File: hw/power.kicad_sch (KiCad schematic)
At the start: 72 parts, among them J1 Ext_Power, J11 PEN_SEL, J2 USB_C_Receptacle_USB2.0, J3 Jtag_Master, J9 Expansion, Q1 Si3477, Q2 Si3477, U1 TLV62569DDC, U16 74LVC1G32, U2 TLV62569DDC, U3 TLV62569DDC, U4 FT240XS

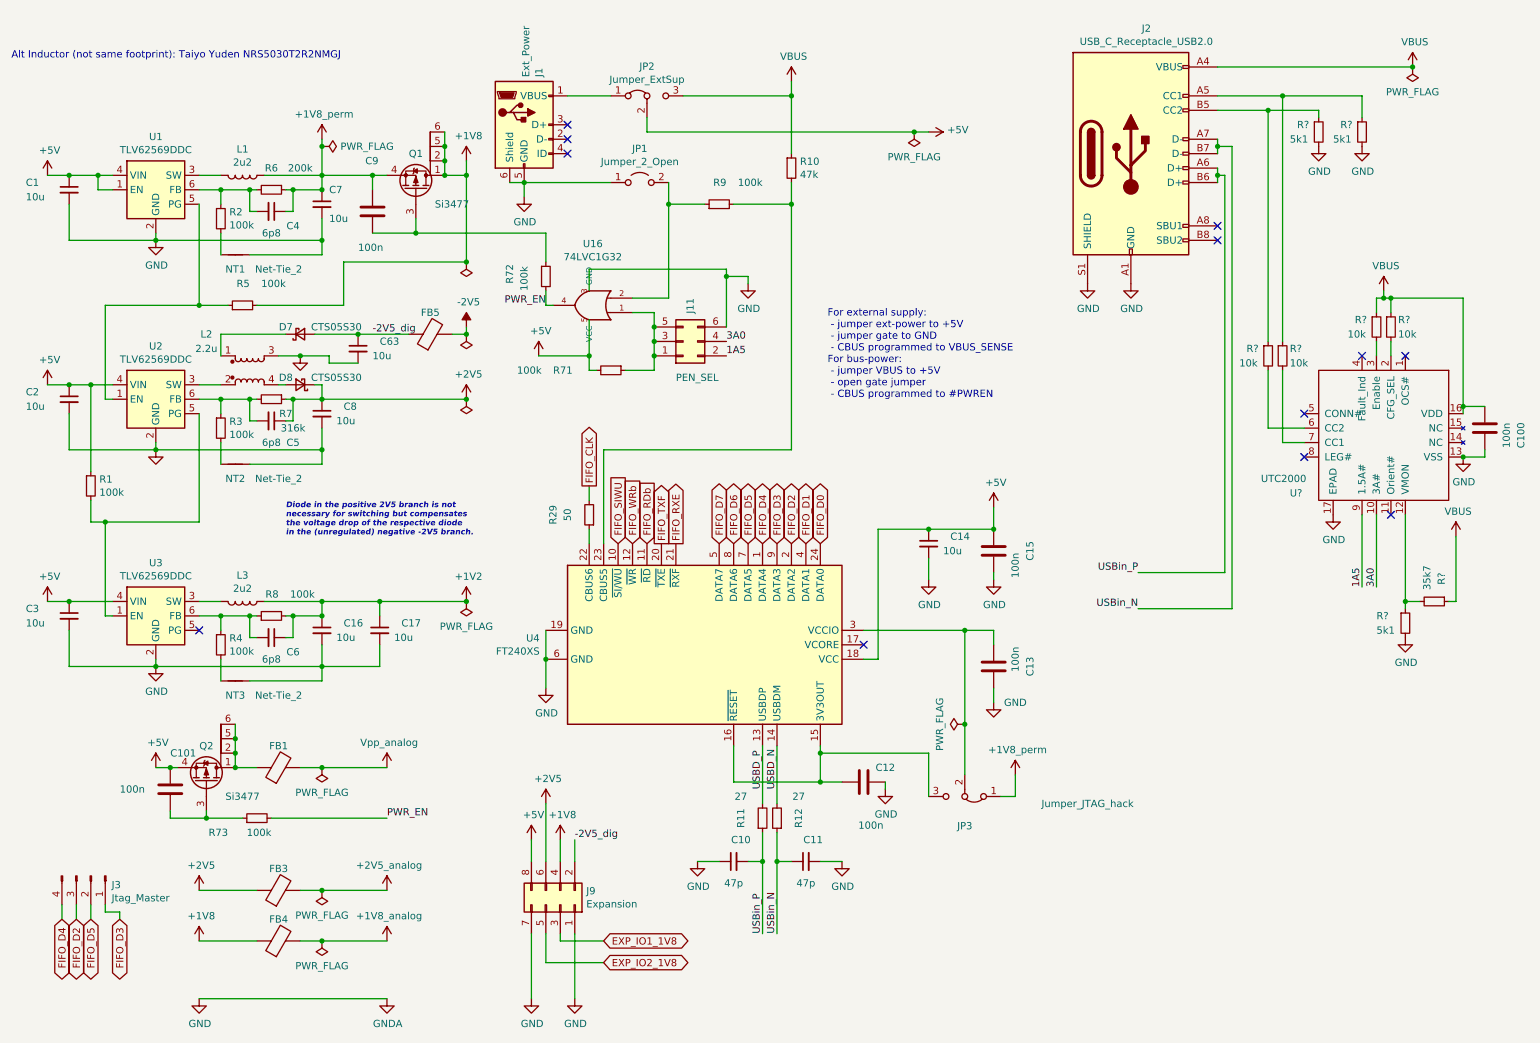
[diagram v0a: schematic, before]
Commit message: basic schematic, started layout (placing first components)
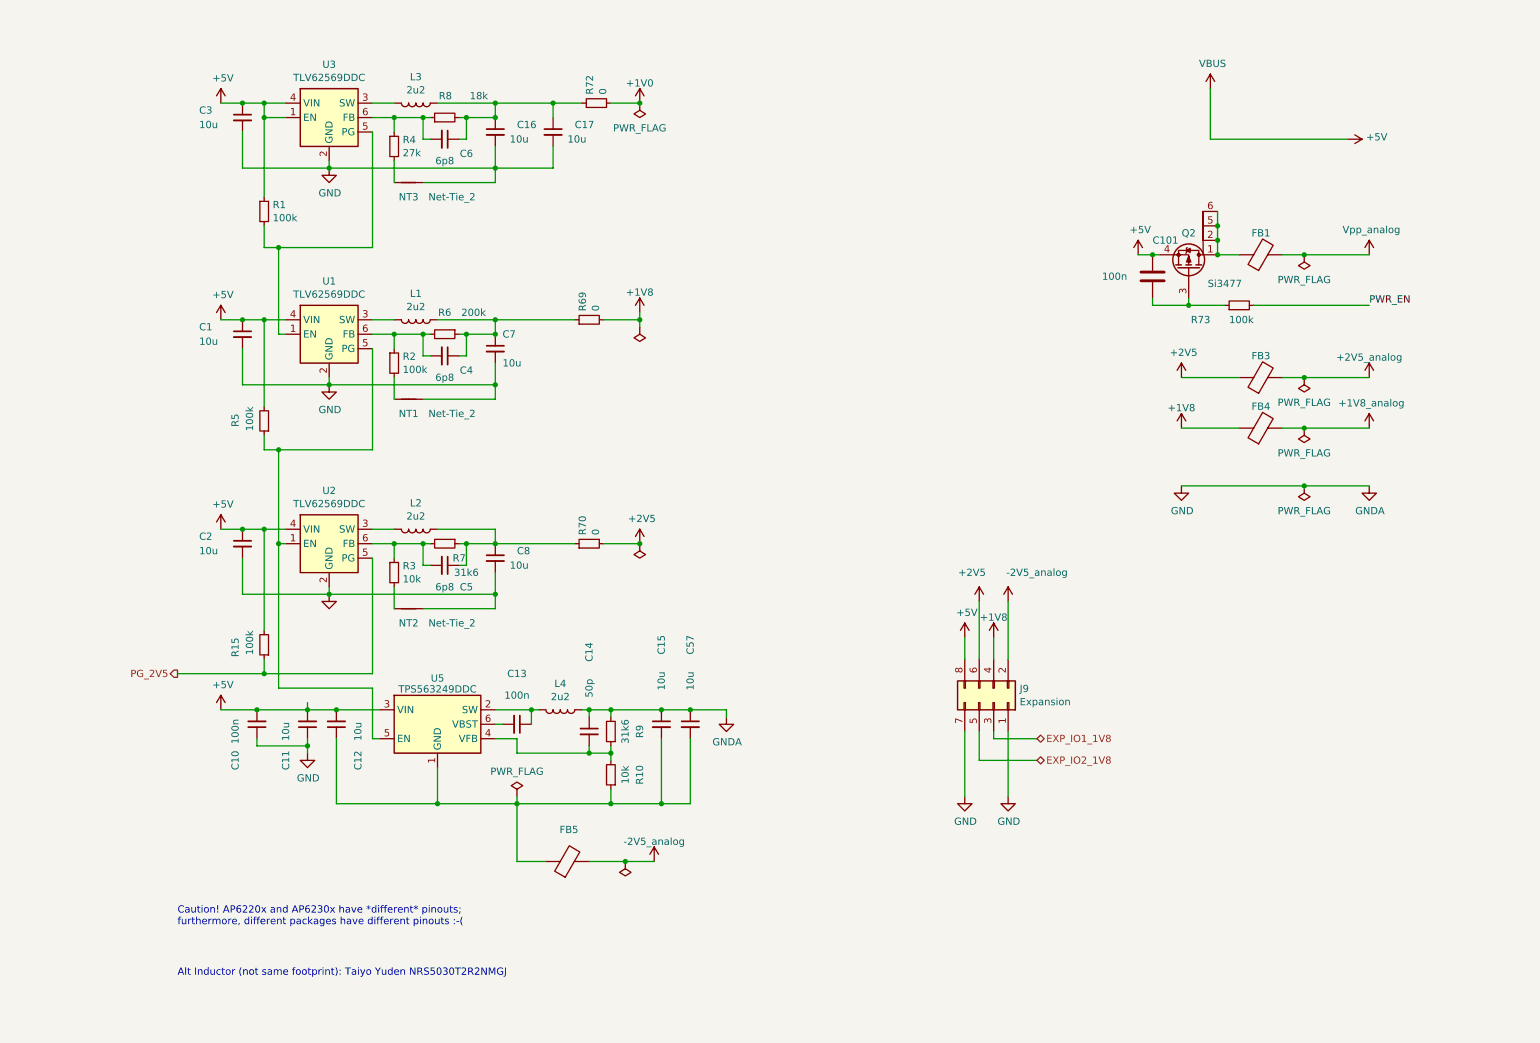
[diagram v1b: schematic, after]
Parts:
- removed C100, C12, C13, C15, C9: 100n, Capacitor_SMD:C_0603_1608Metric, symbol fmc:100nF_603
- removed C63: 10u, Capacitor_SMD:C_1206_3216Metric, symbol Device:C_Small
- removed D7: CTS05S30, proj_footprints:sod323, symbol Device:D_Schottky_Small
- removed D8: CTS05S30, proj_footprints:sod323-special, symbol Device:D_Schottky_Small
- removed J1: Ext_Power, Connector_USB:USB_Micro-B_Molex-105017-0001, symbol Connector:USB_B_Micro
- removed J11: PEN_SEL, Connector_PinHeader_2.54mm:PinHeader_2x03_P2.54mm_Vertical, symbol Connector_Generic:Conn_02x03_Odd_Even
- removed J2: USB_C_Receptacle_USB2.0, proj_footprints:USB_C_Receptacle_GCT_USB4085_smaller_holes, symbol Connector:USB_C_Receptacle_USB2.0
- removed J3: Jtag_Master, Connector_PinHeader_2.54mm:PinHeader_1x04_P2.54mm_Vertical, symbol usbadc-rescue:Conn_01x04_Male-Connector
- removed JP1: Jumper_2_Open, Connector_PinHeader_2.54mm:PinHeader_1x02_P2.54mm_Vertical, symbol Jumper:Jumper_2_Open
- removed JP2: Jumper_ExtSup, Connector_PinHeader_2.54mm:PinHeader_1x03_P2.54mm_Vertical, symbol usbadc-rescue:Jumper_3_Bridged12-Jumper
- removed JP3: Jumper_JTAG_hack, Connector_PinHeader_2.54mm:PinHeader_1x03_P2.54mm_Vertical, symbol usbadc-rescue:Jumper_3_Bridged12-Jumper
- removed L2: 2.2u, proj_footprints:L_Taiyo-Yuden_NR-50xx+bourns0703, symbol Device:L_Coupled_1324
- removed Q1: Si3477, Package_TO_SOT_SMD:TSOT-23-6, symbol fmc:Q_PMOS_DDGSDD
- removed R11, R12: 27, Resistor_SMD:R_0603_1608Metric, symbol Device:R_Small
- removed R29: 50, Resistor_SMD:R_0402_1005Metric, symbol Device:R_Small
- removed R71: 100k, Resistor_SMD:R_0603_1608Metric, symbol Device:R_Small
- removed R? (x4): 10k, Resistor_SMD:R_0603_1608Metric, symbol Device:R_Small
- removed R? (x3): 5k1, Resistor_SMD:R_0603_1608Metric, symbol Device:R_Small
- removed R?: 35k7, Resistor_SMD:R_0603_1608Metric, symbol Device:R_Small
- removed U16: 74LVC1G32, Package_TO_SOT_SMD:SOT-353_SC-70-5, symbol fmc:74LVC1G32
- removed U4: FT240XS, Package_SO:SSOP-24_3.9x8.7mm_P0.635mm, symbol fmc:FT240XS
- removed U?: UTC2000, Package_DFN_QFN:QFN-16-1EP_3x3mm_P0.5mm_EP1.75x1.75mm_ThermalVias, symbol fmc:UTC2000
- added C12, C15, C57: 10u, Capacitor_SMD:C_1206_3216Metric, symbol Device:C_Small
- added C13: 100n, Capacitor_SMD:C_0603_1608Metric, symbol Device:C_Small
- added L2, L4: 2u2, Inductor_SMD:L_Taiyo-Yuden_NR-50xx, symbol Device:L
- added R15: 100k, Resistor_SMD:R_0603_1608Metric, symbol Device:R_Small
- added R69, R70: 0, Resistor_SMD:R_0603_1608Metric, symbol Device:R_Small
- added U5: TPS563249DDC, Package_TO_SOT_SMD:SOT-23-6, symbol Regulator_Switching:TPS563240DDC
- C10: value 47p -> 100n; Manufacturer Wurth -> (none); Part 885012006055 -> (none)
- C11: value 47p -> 10u; footprint Capacitor_SMD:C_0603_1608Metric -> Capacitor_SMD:C_1206_3216Metric; Manufacturer Wurth -> (none); Part 885012006055 -> (none)
- C14: value 10u -> 50p; footprint Capacitor_SMD:C_1206_3216Metric -> Capacitor_SMD:C_0603_1608Metric; Manufacturer TDK -> (none); Part CNC5L1X7R1C106K160AE -> (none)
- FB1, FB3, FB4, FB5: symbol usbadc-rescue:Ferrite_Bead-Device -> Device:FerriteBead
- NT1, NT2, NT3: symbol usbadc-rescue:Net-Tie_2-Device -> Device:NetTie_2
- R10: value 47k -> 10k; Manufacturer Yageo -> (none); Part RC0603FR-07100KL -> (none)
- R3: value 100k -> 10k
- R4: value 100k -> 27k
- R7: value 316k -> 31k6
- R72: value 100k -> 0
- R8: value 100k -> 18k
- R9: value 100k -> 31k6; Manufacturer Yageo -> (none); Part RC0603FR-07100KL -> (none)
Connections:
- net +1V2 is gone; now on an unnamed net: C16.1, C17.1, C6.1, L3.1, R8.2
- net USBin_N is gone; now on net GND: C11.1
- net USBin_P is gone; now on net +5V: C10.2
- net VBUS is gone; now on an unnamed net: R10.1
- net +1V8: now also R69.2; no longer R5.2
- net +2V5: now also R70.2; no longer C5.1, C8.1, R7.1
- net +5V: now also C11.2, R5.2, U3.1 (EN), C12.2, R15.2, U5.3 (VIN); no longer C14.1, U1.1 (EN)
- net GND: now also C14.1, R9.2, C15.1, C57.1, L4.1; no longer C11.2, C14.2
- net PWR_EN: no longer R72.2
- net at R5.1, U1.5 (PG), U2.1 (EN): now also U5.5 (EN)
- net at U2.3 (SW): now also L2.2
- net at U3.5 (PG): now also R1.2, U1.1 (EN)
- net at R9.1: now also C14.2, R10.2, U5.4 (VFB)
- net +1V8_perm: no longer names the net of C4.1, C7.1, L1.1, R6.1
- net +1V8_perm: now also R69.1
- net -2V5 renamed -2V5_analog
- net -2V5_analog: now also J9.2 (Pin_2)
- net -2V5_dig: no longer names the net of FB5.1
- net -2V5_dig: now also C12.1, C15.2, C57.2, U5.1 (GND); no longer J9.2 (Pin_2)
- new net: C5.1, C8.1, L2.1, R7.1, R70.1
- new net: C13.1, L4.2, U5.2 (SW)
- new net: C13.2, U5.6 (VBST)
- new net +1V0: R72.2
- new net PG_2V5: R15.1, U2.5 (PG)
- no-connect marks 12 -> 0
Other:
- note added: "Caution! AP6220x and AP6230x have *different* pinouts; furthermore, different packages have different pinouts :-("
- note removed: "Diode in the positive 2V5 branch is not necessary for switching but compensates the voltage drop of the respective diode in the (unregulated) negative -2V5 branch."
- note removed: "For external supply: - jumper ext-power to +5V - jumper gate to GND - CBUS programmed to VBUS_SENSE For bus-power: - jumper VBUS to +5V - open gate jumper - CBUS programmed to #PWREN"
- moved on the sheet: C1, C101, C16, C17, C2, C3, C4, C5, C6, C7, C8, FB1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

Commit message: WIP - a lot already laid out.
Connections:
- net +5V_switched: now reaches FB1.1, Q2.1 (D), Q2.2 (D), Q2.5 (D), Q2.6 (D)
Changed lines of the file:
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@@
   (junction (at 214.63 58.42) (diameter 0) (color 0 0 0 0)
   )
+  (junction (at 226.06 50.8) (diameter 0) (color 0 0 0 0)
+  )
   (junction (at 58.42 132.08) (diameter 0) (color 0 0 0 0)
   )
@@
     (stroke (width 0) (type default))
   )
+  (wire (pts (xy 226.06 50.8) (xy 252.73 50.8))
+    (stroke (width 0) (type default))
+  )
   (wire (pts (xy 114.3 138.43) (xy 115.57 138.43))
     (stroke (width 0) (type default))
@@
   )
   (wire (pts (xy 99.06 138.43) (xy 105.41 138.43))
+    (stroke (width 0) (type default))
+  )
+  (wire (pts (xy 252.73 50.8) (xy 252.73 48.895))
     (stroke (width 0) (type default))
   )
@@
         )
       )
+    )
+  )
+  (symbol (lib_id "fmc:+5V_switched") (at 252.73 48.895 0) (unit 1)
+    (in_bom yes) (on_board yes) (dnp no) (fields_autoplaced)
+    (property "Reference" "#PWR09" (at 252.73 52.705 0)
+      (effects (font (size 1.27 1.27)) hide)
+    )
+    (property "Value" "+5V_switched" (at 252.73 45.3931 0)
+      (effects (font (size 1.27 1.27)))
+    )
+    (property "Footprint" "" (at 252.73 48.895 0)
+      (effects (font (size 1.27 1.27)) hide)
+    )
+    (property "Datasheet" "" (at 252.73 48.895 0)
+      (effects (font (size 1.27 1.27)) hide)
+    )
+    (pin "1")
+    (instances
+      (project "usbadc"
+        (path "/7c8a1f8d-8834-4c9b-aaae-1f231e9b09a1/00000000-0000-0000-0000-00006086f2e3"
+          (reference "#PWR09") (unit 1)
+        )
+      )

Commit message: layout finished (draft)
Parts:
- removed C101: 100n, Capacitor_SMD:C_0603_1608Metric, symbol fmc:100nF_603
- removed C17: 10u, Capacitor_SMD:C_1206_3216Metric, symbol Device:C_Small
- removed NT1, NT2, NT3: Net-Tie_2, NetTie:NetTie-2_SMD_Pad0.5mm, symbol Device:NetTie_2
- removed Q2: Si3477, Package_TO_SOT_SMD:TSOT-23-6, symbol fmc:Q_PMOS_DDGSDD
- removed R70: 0, Resistor_SMD:R_0603_1608Metric, symbol Device:R_Small
- added C17: 100n, Capacitor_SMD:C_0603_1608Metric, symbol fmc:100nF_603
- added C28: 10u, Capacitor_SMD:C_1206_3216Metric, symbol Device:C_Small
- added Q8: DMC2053UVT, Package_TO_SOT_SMD:TSOT-23-6, symbol Transistor_FET:DMC2053UVT
- L1, L2, L3, L4: value 2u2 -> 1u5; footprint Inductor_SMD:L_Taiyo-Yuden_NR-50xx -> Inductor_SMD:L_1008_2520Metric; Manufacturer Bourns -> (none); Part SRN8040TA-2R2Y -> (none)
- U1, U2, U3: value TLV62569DDC -> RT8096B; Manufacturer Texas Instruments -> Richtek; Part TLV62569PDDC -> RT8096B
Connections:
- net +1V8: now also J9.6 (Pin_6); no longer J9.4 (Pin_4)
- net +1V8_analog: now also C17.2, C28.1
- net +2V5_analog: now also J9.4 (Pin_4)
- net +5V: now also R73.1, Q8.2 (S)
- net +5V_switched: now also Q8.4 (D)
- net GND: now also R2.2, R3.2, R4.2, C17.1, C28.2, Q8.5 (S)
- net at C5.1, C8.1, L2.1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: now also FB3.1
- removed net +2V5: FB3.1, J9.6 (Pin_6)
- net PG_2V5 renamed 5V_EN
- net 5V_EN: now also Q8.1 (G)
- net PWR_EN: no longer names the net of R73.2
- net PWR_EN: now also Q8.3 (G), Q8.6 (D)
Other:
- note removed: "Alt Inductor (not same footprint): Taiyo Yuden NRS5030T2R2NMGJ"
- moved on the sheet: FB3, R73

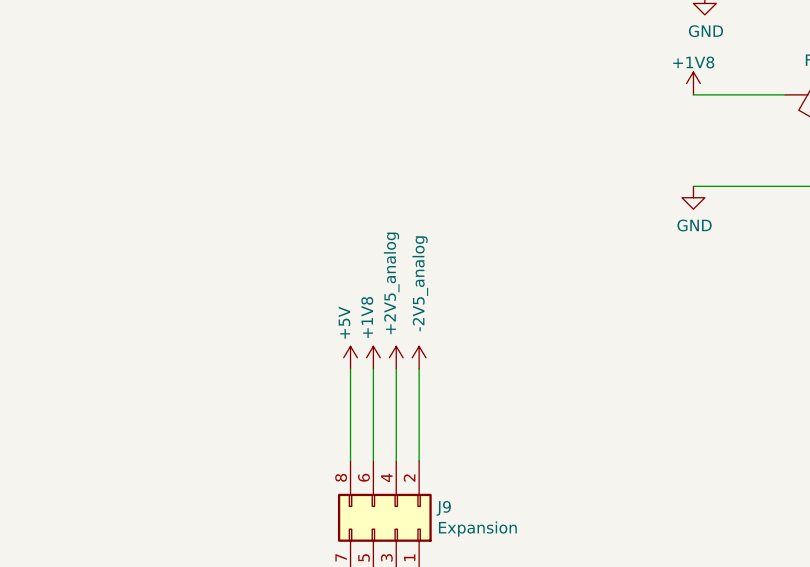
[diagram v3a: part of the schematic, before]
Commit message: finished routing; DRC passes (except for 1 hole violation at push-button)
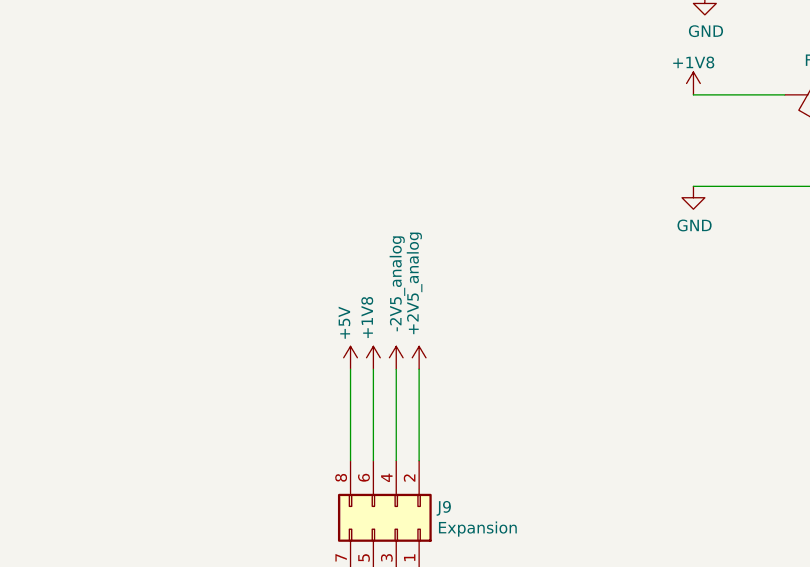
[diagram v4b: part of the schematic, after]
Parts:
- C1, C16, C2, C3, C7, C8: Manufacturer TDK -> (none); Part CNC5L1X7R1C106K160AE -> (none)
- C17: Manufacturer Murata -> (none); Part GCJ188R71E104KA12D -> (none)
- R1, R15, R2, R3, R4, R5, R69, R72, R73, R8: Manufacturer Yageo -> (none); Part RC0603FR-07100KL -> (none)
- R6: Manufacturer Panasonic -> (none); Part ERJ-3EKF2003V -> (none)
- R7: Manufacturer Yageo -> (none); Part RC0603FR-07316KL -> (none)
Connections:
- net +2V5_analog: now also J9.2 (Pin_2); no longer J9.4 (Pin_4)
- net -2V5_analog: now also J9.4 (Pin_4); no longer J9.2 (Pin_2)

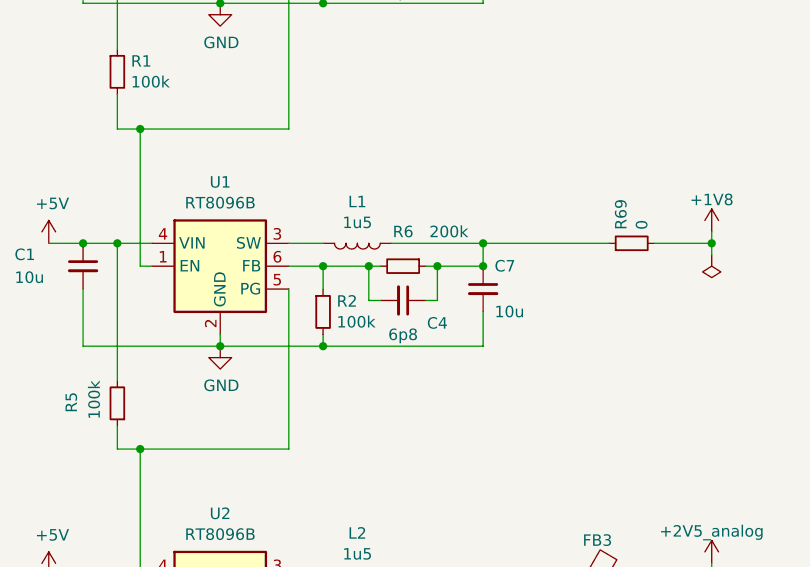
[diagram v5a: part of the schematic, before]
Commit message: standardized resistor/capacitor values
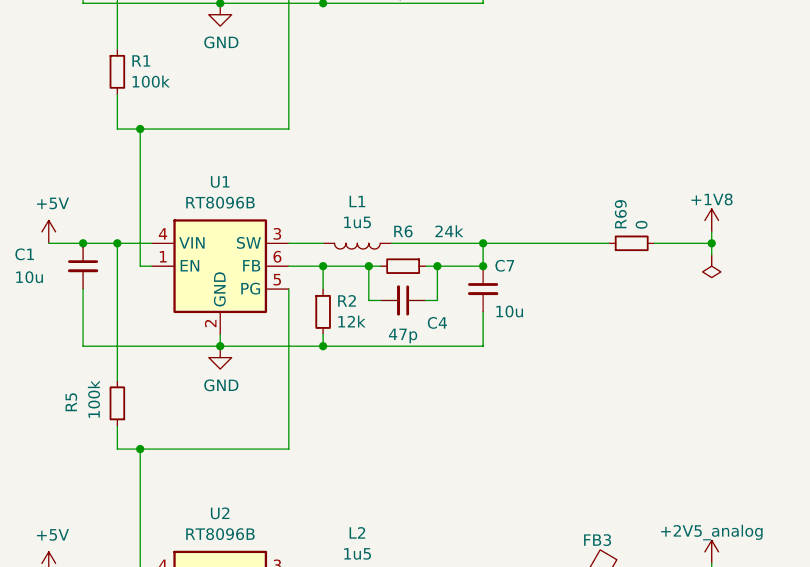
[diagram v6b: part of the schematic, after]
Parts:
- C4: value 6p8 -> 47p
- R2: value 100k -> 12k
- R6: value 200k -> 24k
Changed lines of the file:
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@@
       (effects (font (size 1.27 1.27)) (justify left))
     )
-    (property "Value" "100k" (at 82.7786 78.613 0)
+    (property "Value" "12k" (at 82.7786 78.613 0)
       (effects (font (size 1.27 1.27)) (justify left))
     )
@@
       (effects (font (size 1.27 1.27)))
     )
-    (property "Value" "200k" (at 95.25 68.58 90)
+    (property "Value" "24k" (at 95.25 68.58 90)
       (effects (font (size 1.27 1.27)))
     )
@@
       (effects (font (size 1.27 1.27)))
     )
-    (property "Value" "6p8" (at 90.17 80.01 90)
+    (property "Value" "47p" (at 90.17 80.01 90)
       (effects (font (size 1.27 1.27)))
     )
